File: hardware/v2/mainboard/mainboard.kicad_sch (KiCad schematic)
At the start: 19 parts, among them J1 LEG1_RJ11, J2 LEG2_RJ11, J3 LEG3_RJ11, J4 LEG4_RJ11, J5 LEG5_RJ11, J6 LEG6_RJ11, J7 SBEC_5V_IN, J8 3V3_REG_MODULE, J9 IMU_I2C, U1 ESP32-WROOM-32D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

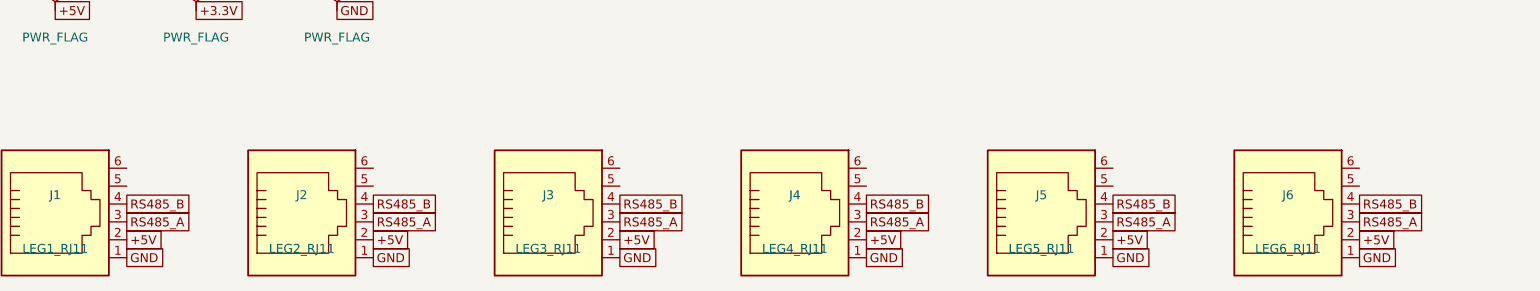
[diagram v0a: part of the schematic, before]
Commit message: Update V2 board schematics and footprints
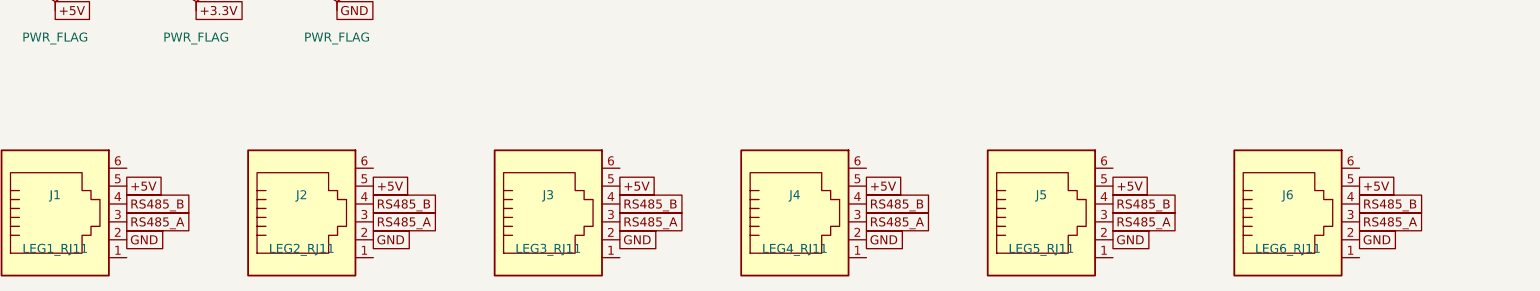
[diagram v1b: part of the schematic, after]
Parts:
- C1, C2, C3, C4: footprint (none) -> Capacitor_SMD:C_0805_2012Metric
- D1: footprint (none) -> LED_SMD:LED_0805_2012Metric
- J1, J2, J3, J4, J5, J6: footprint (none) -> Connector_RJ:RJ25_Wayconn_MJEA-660X1_Horizontal
- J9: footprint (none) -> Connector_PinHeader_2.54mm:PinHeader_1x05_P2.54mm_Vertical
- R1, R2, R3: footprint (none) -> Resistor_SMD:R_0805_2012Metric
- U1: footprint (none) -> Custom:ESP32_Dev_Board
- U2: footprint (none) -> Package_SO:SOIC-8_3.9x4.9mm_P1.27mm
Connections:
- net +5V: now also J1.5, J2.5, J3.5, J4.5, J5.5, J6.5; no longer J1.2, J2.2, J3.2, J4.2, J5.2, J6.2
- net GND: now also J1.2, J2.2, J3.2, J4.2, J5.2, J6.2; no longer J1.1, J2.1, J3.1, J4.1, J5.1, J6.1
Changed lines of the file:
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@@
 			)
 		)
-		(property "Footprint" ""
+		(property "Footprint" "Custom:ESP32_Dev_Board"
 			(at 130 95 0)
 			(effects
@@
 			)
 		)
-		(property "Footprint" ""
+		(property "Footprint" "Resistor_SMD:R_0805_2012Metric"
 			(at 105 80 0)
 			(effects
@@
 			)
 		)
-		(property "Footprint" ""
+		(property "Footprint" "Package_SO:SOIC-8_3.9x4.9mm_P1.27mm"
 			(at 195 95 0)
 			(effects
@@
 			)
 		)
-		(property "Footprint" ""
+		(property "Footprint" "Resistor_SMD:R_0805_2012Metric"
 			(at 220 95 0)
 			(effects
@@
 			)
 		)
-		(property "Footprint" ""
+		(property "Footprint" "Connector_PinHeader_2.54mm:PinHeader_1x05_P2.54mm_Vertical"
 			(at 70 120 0)
 			(effects
@@
 			)
 		)
-		(property "Footprint" ""
+		(property "Footprint" "Capacitor_SMD:C_0805_2012Metric"
 			(at 50 110 0)
 			(effects
@@
 			)
 		)
-		(property "Footprint" ""
+		(property "Footprint" "Capacitor_SMD:C_0805_2012Metric"
 			(at 150 125 0)
 			(effects
@@
 			)
 		)
-		(property "Footprint" ""
+		(property "Footprint" "Capacitor_SMD:C_0805_2012Metric"
 			(at 175 125 0)
 			(effects
@@
 			)
 		)
-		(property "Footprint" ""
+		(property "Footprint" "Capacitor_SMD:C_0805_2012Metric"
 			(at 90 125 0)
 			(effects
@@
 			)
 		)
-		(property "Footprint" ""
+		(property "Footprint" "Resistor_SMD:R_0805_2012Metric"
 			(at 245 55 0)
 			(effects
@@
 			)
 		)
-		(property "Footprint" ""
+		(property "Footprint" "LED_SMD:LED_0805_2012Metric"
 			(at 245 70 0)
 			(effects
@@
 			)
 		)
-		(property "Footprint" ""
+		(property "Footprint" "Connector_RJ:RJ25_Wayconn_MJEA-660X1_Horizontal"
 			(at 40 175 0)
 			(effects
@@
 	(global_label "GND"
 		(shape passive)
-		(at 50.16 180.08 0)
+		(at 50.16 177.54 0)
+		(fields_autoplaced yes)
+		(effects
+			(font
+				(size 1.27 1.27)
+			)
+			(justify left)
+		)
+	)
+	(global_label "RS485_A"
+		(shape passive)
+		(at 50.16 175 0)
+		(fields_autoplaced yes)
+		(effects
+			(font
+				(size 1.27 1.27)
+			)
+			(justify left)
+		)
+	)
+	(global_label "RS485_B"
+		(shape passive)
+		(at 50.16 172.46 0)
 		(fields_autoplaced yes)
 		(effects
@@
 	(global_label "+5V"
 		(shape passive)
-		(at 50.16 177.54 0)
-		(fields_autoplaced yes)
-		(effects
-			(font
-				(size 1.27 1.27)
-			)
-			(justify left)
-		)
-	)
-	(global_label "RS485_A"
-		(shape passive)
-		(at 50.16 175 0)
-		(fields_autoplaced yes)
-		(effects
-			(font
-				(size 1.27 1.27)
-			)
-			(justify left)
-		)
-	)
-	(global_label "RS485_B"
-		(shape passive)
-		(at 50.16 172.46 0)
+		(at 50.16 169.92 0)
 		(fields_autoplaced yes)
 		(effects
@@
 			)
 		)
-		(property "Footprint" ""
+		(property "Footprint" "Connector_RJ:RJ25_Wayconn_MJEA-660X1_Horizontal"
 			(at 75 175 0)
 			(effects
@@
 	(global_label "GND"
 		(shape passive)
-		(at 85.16 180.08 0)
+		(at 85.16 177.54 0)
+		(fields_autoplaced yes)
+		(effects
+			(font
+				(size 1.27 1.27)
+			)
+			(justify left)
+		)
+	)
+	(global_label "RS485_A"
+		(shape passive)
+		(at 85.16 175 0)
+		(fields_autoplaced yes)
+		(effects
+			(font
+				(size 1.27 1.27)
+			)
+			(justify left)
+		)
+	)
+	(global_label "RS485_B"
+		(shape passive)
+		(at 85.16 172.46 0)
 		(fields_autoplaced yes)
 		(effects
@@
 	(global_label "+5V"
 		(shape passive)
-		(at 85.16 177.54 0)
-		(fields_autoplaced yes)
-		(effects
-			(font
-				(size 1.27 1.27)
-			)
-			(justify left)
-		)
-	)
-	(global_label "RS485_A"
-		(shape passive)
-		(at 85.16 175 0)
-		(fields_autoplaced yes)
-		(effects
-			(font
-				(size 1.27 1.27)
-			)
-			(justify left)
-		)
-	)
-	(global_label "RS485_B"
-		(shape passive)
-		(at 85.16 172.46 0)
+		(at 85.16 169.92 0)
 		(fields_autoplaced yes)
 		(effects
@@
 			)
 		)
-		(property "Footprint" ""
+		(property "Footprint" "Connector_RJ:RJ25_Wayconn_MJEA-660X1_Horizontal"
 			(at 110 175 0)
 			(effects
@@
 	(global_label "GND"
 		(shape passive)
-		(at 120.16 180.08 0)
+		(at 120.16 177.54 0)
+		(fields_autoplaced yes)
+		(effects
+			(font
+				(size 1.27 1.27)
+			)
+			(justify left)
+		)
+	)
+	(global_label "RS485_A"
+		(shape passive)
+		(at 120.16 175 0)
+		(fields_autoplaced yes)
+		(effects
+			(font
+				(size 1.27 1.27)
+			)
+			(justify left)
+		)
+	)
+	(global_label "RS485_B"
+		(shape passive)
+		(at 120.16 172.46 0)
 		(fields_autoplaced yes)
 		(effects
@@
 	(global_label "+5V"
 		(shape passive)
-		(at 120.16 177.54 0)
-		(fields_autoplaced yes)
-		(effects
-			(font
-				(size 1.27 1.27)
-			)
-			(justify left)
-		)
-	)
-	(global_label "RS485_A"
-		(shape passive)
-		(at 120.16 175 0)
-		(fields_autoplaced yes)
-		(effects
-			(font
-				(size 1.27 1.27)
-			)
-			(justify left)
-		)
-	)
-	(global_label "RS485_B"
-		(shape passive)
-		(at 120.16 172.46 0)
+		(at 120.16 169.92 0)
 		(fields_autoplaced yes)
 		(effects
@@
 			)
 		)
-		(property "Footprint" ""
+		(property "Footprint" "Connector_RJ:RJ25_Wayconn_MJEA-660X1_Horizontal"
 			(at 145 175 0)
 			(effects
@@
 	(global_label "GND"
 		(shape passive)
-		(at 155.16 180.08 0)
+		(at 155.16 177.54 0)
+		(fields_autoplaced yes)
+		(effects
+			(font
+				(size 1.27 1.27)
+			)
+			(justify left)
+		)
+	)
+	(global_label "RS485_A"
+		(shape passive)
+		(at 155.16 175 0)
+		(fields_autoplaced yes)
+		(effects
+			(font
+				(size 1.27 1.27)
+			)
+			(justify left)
+		)
+	)
+	(global_label "RS485_B"
+		(shape passive)
+		(at 155.16 172.46 0)
 		(fields_autoplaced yes)
 		(effects
@@
 	(global_label "+5V"
 		(shape passive)
-		(at 155.16 177.54 0)
-		(fields_autoplaced yes)
-		(effects
-			(font
-				(size 1.27 1.27)
-			)
-			(justify left)
-		)
-	)
-	(global_label "RS485_A"
-		(shape passive)
-		(at 155.16 175 0)
-		(fields_autoplaced yes)
-		(effects
-			(font
-				(size 1.27 1.27)
-			)
-			(justify left)
-		)
-	)
-	(global_label "RS485_B"
-		(shape passive)
-		(at 155.16 172.46 0)
+		(at 155.16 169.92 0)
 		(fields_autoplaced yes)
 		(effects
@@
 			)
 		)
-		(property "Footprint" ""
+		(property "Footprint" "Connector_RJ:RJ25_Wayconn_MJEA-660X1_Horizontal"
 			(at 180 175 0)
 			(effects
@@
 	(global_label "GND"
 		(shape passive)
-		(at 190.16 180.08 0)
+		(at 190.16 177.54 0)
+		(fields_autoplaced yes)
+		(effects
+			(font
+				(size 1.27 1.27)
+			)
+			(justify left)
+		)
+	)
+	(global_label "RS485_A"
+		(shape passive)
+		(at 190.16 175 0)
+		(fields_autoplaced yes)
+		(effects
+			(font
+				(size 1.27 1.27)
+			)
+			(justify left)
+		)
+	)
+	(global_label "RS485_B"
+		(shape passive)
+		(at 190.16 172.46 0)
 		(fields_autoplaced yes)
 		(effects
@@
 	(global_label "+5V"
 		(shape passive)
-		(at 190.16 177.54 0)
-		(fields_autoplaced yes)
-		(effects
-			(font
-				(size 1.27 1.27)
-			)
-			(justify left)
-		)
-	)
-	(global_label "RS485_A"
-		(shape passive)
-		(at 190.16 175 0)
-		(fields_autoplaced yes)
-		(effects
-			(font
-				(size 1.27 1.27)
-			)
-			(justify left)
-		)
-	)
-	(global_label "RS485_B"
-		(shape passive)
-		(at 190.16 172.46 0)
+		(at 190.16 169.92 0)
 		(fields_autoplaced yes)
 		(effects
@@
 			)
 		)
-		(property "Footprint" ""
+		(property "Footprint" "Connector_RJ:RJ25_Wayconn_MJEA-660X1_Horizontal"
 			(at 215 175 0)
 			(effects
@@
 	(global_label "GND"
 		(shape passive)
-		(at 225.16 180.08 0)
+		(at 225.16 177.54 0)
+		(fields_autoplaced yes)
+		(effects
+			(font
+				(size 1.27 1.27)
+			)
+			(justify left)
+		)
+	)
+	(global_label "RS485_A"
+		(shape passive)
+		(at 225.16 175 0)
+		(fields_autoplaced yes)
+		(effects
+			(font
+				(size 1.27 1.27)
+			)
+			(justify left)
+		)
+	)
+	(global_label "RS485_B"
+		(shape passive)
+		(at 225.16 172.46 0)
 		(fields_autoplaced yes)
 		(effects
@@
 	(global_label "+5V"
 		(shape passive)
-		(at 225.16 177.54 0)
-		(fields_autoplaced yes)
-		(effects
-			(font
-				(size 1.27 1.27)
-			)
-			(justify left)
-		)
-	)
-	(global_label "RS485_A"
-		(shape passive)
-		(at 225.16 175 0)
-		(fields_autoplaced yes)
-		(effects
-			(font
-				(size 1.27 1.27)
-			)
-			(justify left)
-		)
-	)
-	(global_label "RS485_B"
-		(shape passive)
-		(at 225.16 172.46 0)
-		(fields_autoplaced yes)
-		(effects
+		(at 225.16 169.92 0)
+		(fields_autoplaced yes)
+		(effects

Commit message: manual fixes for mainboard
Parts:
- C1: footprint Capacitor_SMD:C_0805_2012Metric -> Capacitor_THT:CP_Radial_D4.0mm_P2.00mm
- J7: footprint (none) -> TerminalBlock:TerminalBlock_MaiXu_MX126-5.0-02P_1x02_P5.00mm
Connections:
- net +5V: now also U1.2 (VIN)
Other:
- moved on the sheet: J1, J2, J3, J4, J5, J6, U1, U2

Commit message: revised mainbaord schematics
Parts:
- removed D1: PWR, LED_SMD:LED_0805_2012Metric, symbol Device:LED_Small
- removed J8: 3V3_REG_MODULE, symbol Connector:Conn_01x03_Pin
- removed R3: 1k, Resistor_SMD:R_0805_2012Metric, symbol Device:R_Small
- added C5: 10uF, Capacitor_THT:CP_Radial_D4.0mm_P2.00mm, symbol Device:C_Polarized
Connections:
- net +3.3V: now also C5.1
- net GND: now also C5.2

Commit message: mainboard physical design
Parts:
- removed R2: 10k, Resistor_SMD:R_0805_2012Metric, symbol Device:R_Small
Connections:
- net ESP_EN: no longer names the net of U1.0 (EN)
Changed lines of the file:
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@@
-	)
-	(symbol
-		(lib_id "Device:R_Small")
-		(at 105 80 90)
-		(unit 1)
-		(exclude_from_sim no)
-		(in_bom yes)
-		(on_board yes)
-		(dnp no)
-		(fields_autoplaced yes)
-		(property "Reference" "R2"
-			(at 105 76.19 0)
-			(effects
-				(font
-					(size 1.27 1.27)
-				)
-			)
-		)
-		(property "Value" "10k"
-			(at 105 83.81 0)
-			(effects
-				(font
-					(size 1.27 1.27)
-				)
-			)
-		)
-		(property "Footprint" "Resistor_SMD:R_0805_2012Metric"
-			(at 105 80 0)
-			(effects
-				(font
-					(size 1.27 1.27)
-				)
-				(hide yes)
-			)
-		)
-		(property "Datasheet" "~"
-			(at 105 80 0)
-			(effects
-				(font
-					(size 1.27 1.27)
-				)
-				(hide yes)
-			)
-		)
-		(instances
-			(project ""
-				(path "/4e2dbab2-bc0e-4263-812c-ac23f540fa33"
-					(reference "R2")
-					(unit 1)
-				)
-			)
-		)
-	)
-	(global_label "+3.3V"
-		(shape passive)
-		(at 107.54 80 0)
-		(fields_autoplaced yes)
-		(effects
-			(font
-				(size 1.27 1.27)
-			)
-			(justify left)
-		)
-	)
-	(global_label "ESP_EN"
-		(shape passive)
-		(at 114.76 24.52 0)
-		(fields_autoplaced yes)
-		(effects
-			(font
-				(size 1.27 1.27)
-			)
-			(justify left)
-		)
-	)
-	(global_label "ESP_EN"
-		(shape passive)
-		(at 102.46 80 180)
-		(fields_autoplaced yes)
-		(effects
-			(font
-				(size 1.27 1.27)
-			)
-			(justify right)
-		)
 	)
 	(symbol
